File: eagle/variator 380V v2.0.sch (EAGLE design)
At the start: 31 parts, among them P1 BANANA, P2 BANANA, P3 BANANA, P4 BANANA

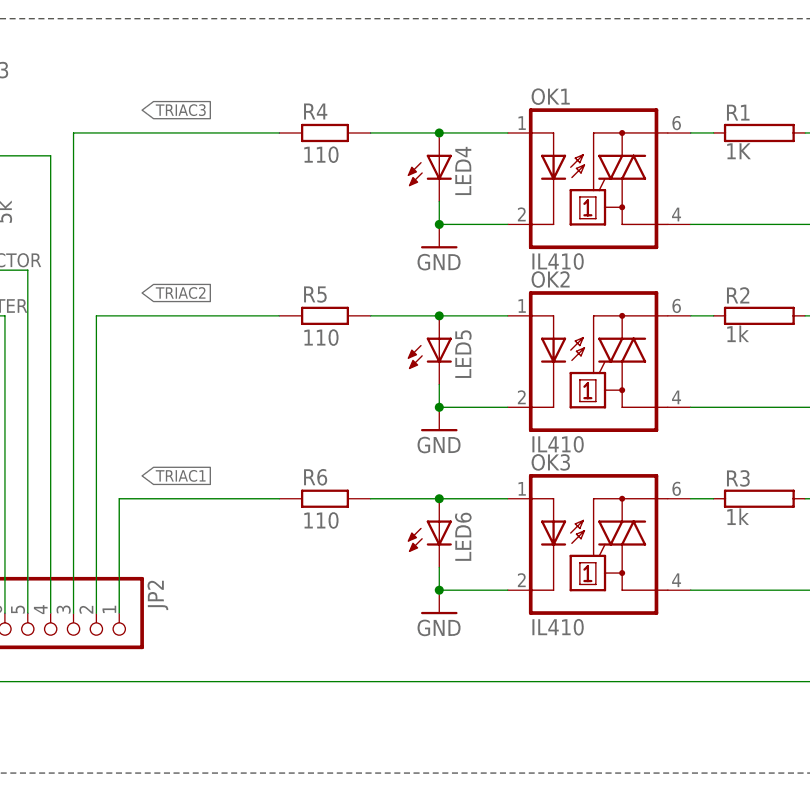
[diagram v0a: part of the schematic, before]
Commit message: Resistenta separate la fiecare led in parte. Led in parallel connection.
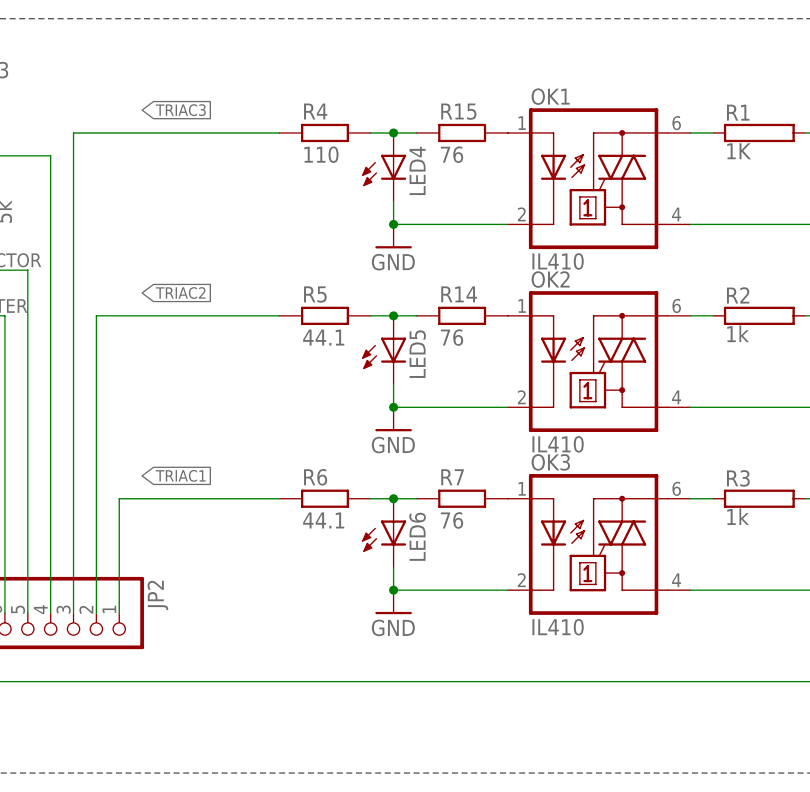
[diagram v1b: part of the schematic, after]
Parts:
- added R14, R15, R7: 76, adi_v1.4:R1206
- R5, R6: value 110 -> 44.1
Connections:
- new net N$12: OK1.A, R15.2
- new net N$8: OK3.A, R7.2
- new net N$9: OK2.A, R14.2
- net N$10: now also R14.1; no longer OK2.A
- net N$11: now also R7.1; no longer OK3.A
- net N$7: now also R15.1; no longer OK1.A
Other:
- moved on the sheet: LED4, LED5, LED6
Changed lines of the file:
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@@
 <part name="R3" library="resistor-power" deviceset="R" device="HPS58" value="1k"/>
 <part name="R4" library="adi_v1.4" deviceset="R" device="1206" value="110"/>
-<part name="R5" library="adi_v1.4" deviceset="R" device="1206" value="110"/>
-<part name="R6" library="adi_v1.4" deviceset="R" device="1206" value="110"/>
+<part name="R5" library="adi_v1.4" deviceset="R" device="1206" value="44.1"/>
+<part name="R6" library="adi_v1.4" deviceset="R" device="1206" value="44.1"/>
 <part name="R8" library="resistor-power" deviceset="R" device="HPS58" value="500k"/>
 <part name="R9" library="resistor-power" deviceset="R" device="HPS58" value="500k"/>
@@
 <part name="U$2" library="Serghei IR station" deviceset="Q8025NH6RP" device=""/>
 <part name="U$3" library="Serghei IR station" deviceset="Q8025NH6RP" device=""/>
+<part name="R7" library="adi_v1.4" deviceset="R" device="1206" value="76"/>
+<part name="R14" library="adi_v1.4" deviceset="R" device="1206" value="76"/>
+<part name="R15" library="adi_v1.4" deviceset="R" device="1206" value="76"/>
 </parts>
 <sheets>
@@
 <instance part="R13" gate="R" x="73.66" y="63.5" rot="R90"/>
 <instance part="GND1" gate="G$1" x="71.12" y="40.64"/>
-<instance part="GND2" gate="G$1" x="124.46" y="58.42"/>
-<instance part="GND3" gate="G$1" x="124.46" y="38.1"/>
-<instance part="GND4" gate="G$1" x="124.46" y="17.78"/>
-<instance part="LED4" gate="G$1" x="124.46" y="68.58"/>
-<instance part="LED5" gate="G$1" x="124.46" y="48.26"/>
-<instance part="LED6" gate="G$1" x="124.46" y="27.94"/>
+<instance part="GND2" gate="G$1" x="119.38" y="58.42"/>
+<instance part="GND3" gate="G$1" x="119.38" y="38.1"/>
+<instance part="GND4" gate="G$1" x="119.38" y="17.78"/>
+<instance part="LED4" gate="G$1" x="119.38" y="68.58"/>
+<instance part="LED5" gate="G$1" x="119.38" y="48.26"/>
+<instance part="LED6" gate="G$1" x="119.38" y="27.94"/>
 <instance part="U$9" gate="G$1" x="202.946" y="46.99" rot="MR180"/>
 <instance part="U$11" gate="G$1" x="203.2" y="67.31" rot="MR180"/>
@@
 <instance part="U$2" gate="G$1" x="187.96" y="43.18" rot="MR180"/>
 <instance part="U$3" gate="G$1" x="187.96" y="22.86" rot="MR180"/>
+<instance part="R7" gate="R" x="127" y="30.48"/>
+<instance part="R14" gate="R" x="127" y="50.8"/>
+<instance part="R15" gate="R" x="127" y="71.12"/>
 </instances>
 <busses>
@@
 <net name="N$7" class="0">
 <segment>
-<pinref part="OK1" gate="G$1" pin="A"/>
 <pinref part="R4" gate="R" pin="2"/>
-<wire x1="132.08" y1="71.12" x2="124.46" y2="71.12" width="0.1524" layer="91"/>
 <pinref part="LED4" gate="G$1" pin="A"/>
-<wire x1="124.46" y1="71.12" x2="116.84" y2="71.12" width="0.1524" layer="91"/>
-<junction x="124.46" y="71.12"/>
+<wire x1="119.38" y1="71.12" x2="116.84" y2="71.12" width="0.1524" layer="91"/>
+<pinref part="R15" gate="R" pin="1"/>
+<junction x="119.38" y="71.12"/>
+<wire x1="119.38" y1="71.12" x2="121.92" y2="71.12" width="0.1524" layer="91"/>
 </segment>
 </net>
 <net name="N$10" class="0">
 <segment>
-<pinref part="OK2" gate="G$1" pin="A"/>
 <pinref part="R5" gate="R" pin="2"/>
-<wire x1="132.08" y1="50.8" x2="124.46" y2="50.8" width="0.1524" layer="91"/>
 <pinref part="LED5" gate="G$1" pin="A"/>
-<wire x1="124.46" y1="50.8" x2="116.84" y2="50.8" width="0.1524" layer="91"/>
-<junction x="124.46" y="50.8"/>
+<wire x1="119.38" y1="50.8" x2="116.84" y2="50.8" width="0.1524" layer="91"/>
+<pinref part="R14" gate="R" pin="1"/>
+<junction x="119.38" y="50.8"/>
+<wire x1="119.38" y1="50.8" x2="121.92" y2="50.8" width="0.1524" layer="91"/>
 </segment>
 </net>
 <net name="N$11" class="0">
 <segment>
-<pinref part="OK3" gate="G$1" pin="A"/>
 <pinref part="R6" gate="R" pin="2"/>
-<wire x1="132.08" y1="30.48" x2="124.46" y2="30.48" width="0.1524" layer="91"/>
 <pinref part="LED6" gate="G$1" pin="A"/>
-<wire x1="124.46" y1="30.48" x2="116.84" y2="30.48" width="0.1524" layer="91"/>
-<junction x="124.46" y="30.48"/>
+<wire x1="119.38" y1="30.48" x2="116.84" y2="30.48" width="0.1524" layer="91"/>
+<pinref part="R7" gate="R" pin="1"/>
+<junction x="119.38" y="30.48"/>
+<wire x1="119.38" y1="30.48" x2="121.92" y2="30.48" width="0.1524" layer="91"/>
 </segment>
 </net>
@@
 <segment>
 <pinref part="OK1" gate="G$1" pin="C"/>
-<wire x1="132.08" y1="60.96" x2="124.46" y2="60.96" width="0.1524" layer="91"/>
-<wire x1="124.46" y1="60.96" x2="124.46" y2="63.5" width="0.1524" layer="91"/>
+<wire x1="132.08" y1="60.96" x2="119.38" y2="60.96" width="0.1524" layer="91"/>
+<wire x1="119.38" y1="60.96" x2="119.38" y2="63.5" width="0.1524" layer="91"/>
 <pinref part="GND2" gate="G$1" pin="GND"/>
-<junction x="124.46" y="60.96"/>
+<junction x="119.38" y="60.96"/>
 <pinref part="LED4" gate="G$1" pin="C"/>
 </segment>
 <segment>
 <pinref part="OK2" gate="G$1" pin="C"/>
-<wire x1="132.08" y1="40.64" x2="124.46" y2="40.64" width="0.1524" layer="91"/>
-<wire x1="124.46" y1="40.64" x2="124.46" y2="43.18" width="0.1524" layer="91"/>
+<wire x1="132.08" y1="40.64" x2="119.38" y2="40.64" width="0.1524" layer="91"/>
+<wire x1="119.38" y1="40.64" x2="119.38" y2="43.18" width="0.1524" layer="91"/>
 <pinref part="GND3" gate="G$1" pin="GND"/>
-<junction x="124.46" y="40.64"/>
+<junction x="119.38" y="40.64"/>
 <pinref part="LED5" gate="G$1" pin="C"/>
 </segment>
 <segment>
 <pinref part="OK3" gate="G$1" pin="C"/>
-<wire x1="132.08" y1="20.32" x2="124.46" y2="20.32" width="0.1524" layer="91"/>
-<wire x1="124.46" y1="20.32" x2="124.46" y2="22.86" width="0.1524" layer="91"/>
+<wire x1="132.08" y1="20.32" x2="119.38" y2="20.32" width="0.1524" layer="91"/>
+<wire x1="119.38" y1="20.32" x2="119.38" y2="22.86" width="0.1524" layer="91"/>
 <pinref part="GND4" gate="G$1" pin="GND"/>
-<junction x="124.46" y="20.32"/>
+<junction x="119.38" y="20.32"/>
 <pinref part="LED6" gate="G$1" pin="C"/>
 </segment>
 </net>
+<net name="N$8" class="0">
+<segment>
+<pinref part="OK3" gate="G$1" pin="A"/>
+<pinref part="R7" gate="R" pin="2"/>
+</segment>
+</net>
+<net name="N$9" class="0">
+<segment>
+<pinref part="OK2" gate="G$1" pin="A"/>
+<pinref part="R14" gate="R" pin="2"/>
+</segment>
+</net>
+<net name="N$12" class="0">
+<segment>
+<pinref part="OK1" gate="G$1" pin="A"/>
+<pinref part="R15" gate="R" pin="2"/>
+</segment>
+</net>
